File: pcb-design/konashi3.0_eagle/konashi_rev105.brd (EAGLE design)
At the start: 33 x 52.1 mm, 35 parts, among them CN1 ZX62-B-5PA(11), CN2 S2B-PH-K-S, CN3 WML-C69, CN4 MA05-2-2, CN7 BK-913, IC1 LP2981-30DBVR, IC2 ZLDO1117G50DITR-ND

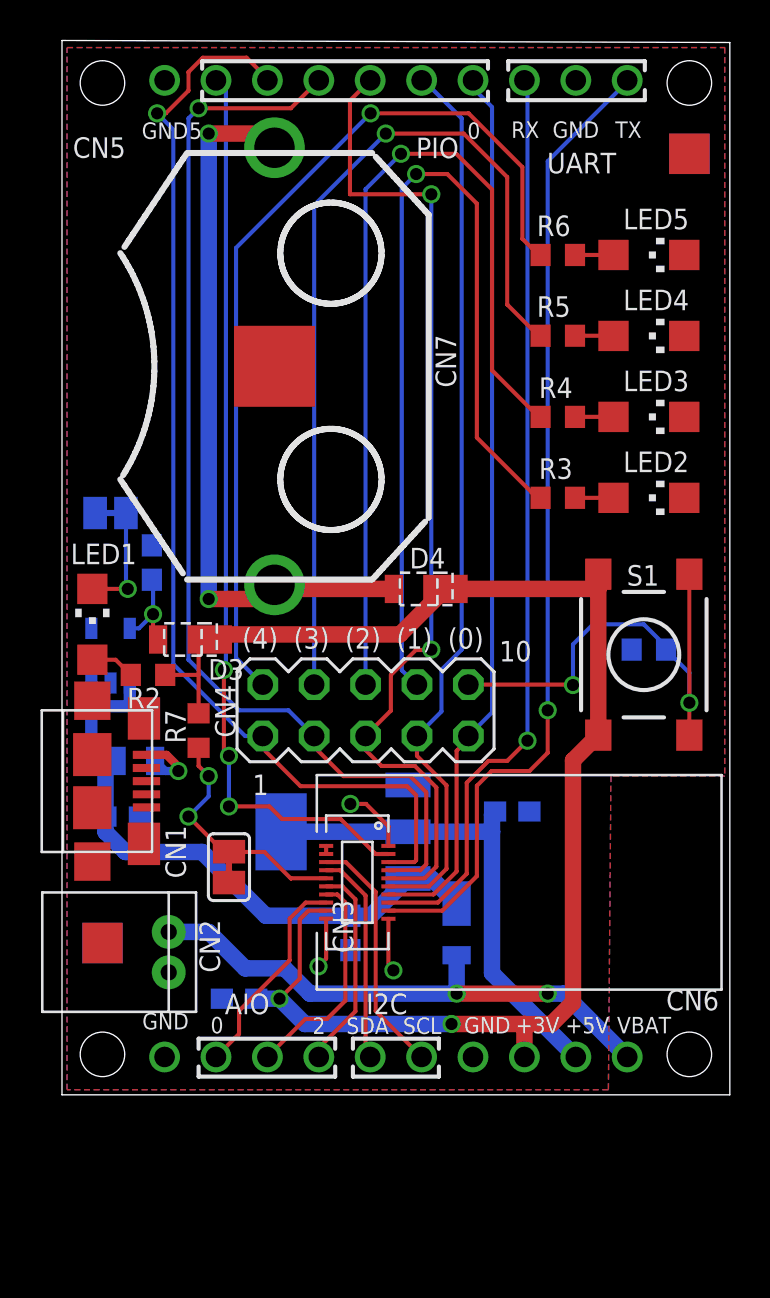
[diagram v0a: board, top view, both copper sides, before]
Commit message: 500kohm追加、ジャンパ用ピンヘッダ変更
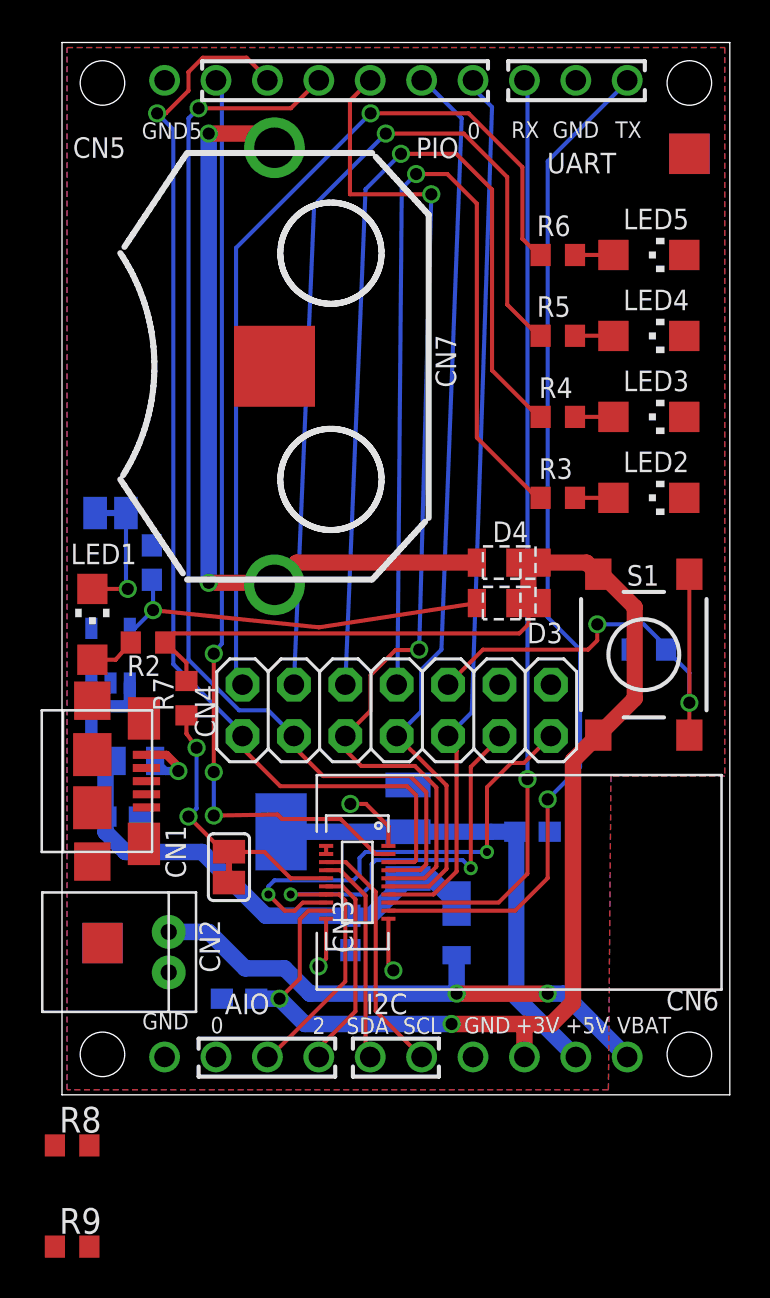
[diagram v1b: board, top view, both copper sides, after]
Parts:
- added R8, R9: 500k, rcl:R0603
- CN4: value MA05-2-2 -> 2X07; device con-std:MA05-2-2 -> konashi_rev105:2X07
- moved D3 15.9 mm to (22.1, 24.3)
- moved D4 4.30 mm to (22.1, 26.3)
- moved R7 1.71 mm to (6.15, 19.6)
- moved R2 1.60 mm to (4.25, 22.4)
- moved C5 1.41 mm to (23.2, 13.0)
- moved CN4 1.00 mm to (14.0, 19.0)
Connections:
- new net N$11: CN4.14, R9.1
- new net N$7: CN4.12, R8.1
- net AIO0: now also CN4.13
- net AIO1: now also CN4.11
- net GND: now also R8.2, R9.2
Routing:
- net AIO1: track 11.0 -> 29.7 mm, vias 0 -> 2
- net N$6: track 4.70 -> 19.2 mm
- net AIO0: track 10.5 -> 23.1 mm, vias 0 -> 2
- net N$4: track 36.3 -> 39.5 mm
- net TX: track 48.7 -> 51.0 mm
- net +3V: track 72.7 -> 74.7 mm
- net PIO2: track 50.1 -> 51.5 mm
- net N$5: track 12.1 -> 13.4 mm
- net RX: track 45.6 -> 46.8 mm
- net PIO5: track 45.1 -> 46.0 mm
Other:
- board size 33 x 52.1 mm -> 33 x 52 mm

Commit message: シルク修正
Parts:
- moved R9 40.3 mm to (24.1, 25.1), flipped to the bottom, turned to 90 degrees
- moved R8 34.8 mm to (21.6, 25.1), flipped to the bottom, turned to 90 degrees
- moved C5 2.40 mm to (23.2, 10.6)
- moved R2 0.80 mm to (4.25, 21.6)
- moved R7 0.60 mm to (6.15, 19.0)
- moved C1 0.40 mm to (4.44, 25.9)
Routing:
- net AIO0: track 23.1 -> 31.9 mm
- net N$7: track 0.00 -> 3.99 mm
- net N$11: track 0.00 -> 3.98 mm
- net PIO4: track 55.1 -> 52.3 mm
- net PIO2: track 51.5 -> 49.0 mm
- net N$23: track 45.3 -> 47.0 mm
- net PIO5: track 46.0 -> 47.7 mm, vias 3 -> 1
- net TX: track 51.0 -> 49.6 mm
- net +3V: track 74.7 -> 75.8 mm
- net GND: track 8.87 -> 7.76 mm
- net N$5: track 13.4 -> 12.5 mm
- net N$4: track 39.5 -> 38.7 mm
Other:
- board text added: "/SCL"
- board text added: "/SDA"
- board text added: "PIO6"
- board text added: "PIO7"
- board text added: "YE-WPC003"
- board text added: "rev. 1.05"
- board text removed: "I2C"
- board text removed: "SCL"
- board text removed: "SDA"
- board text removed: "YE-WPC002"
- board text removed: "rev. 1.03"

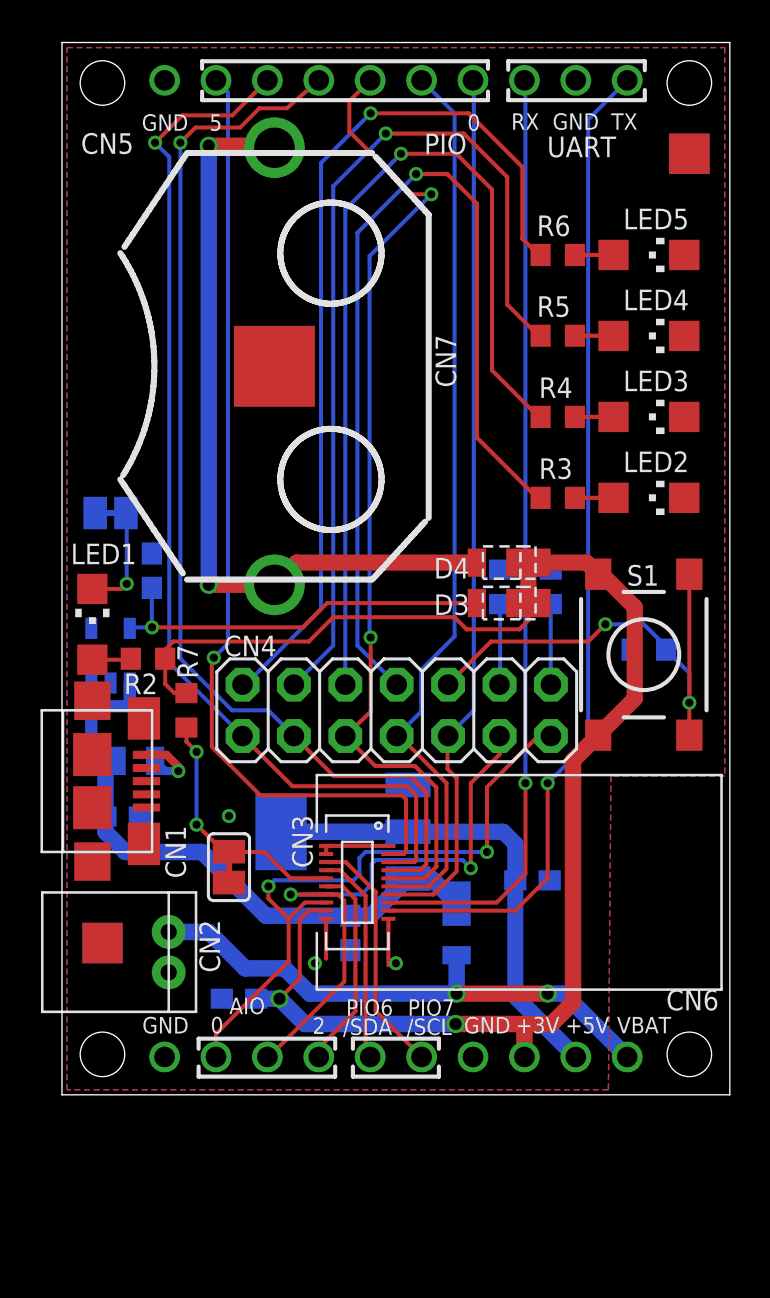
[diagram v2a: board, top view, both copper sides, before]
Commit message: ジャンパピンシルク追加等
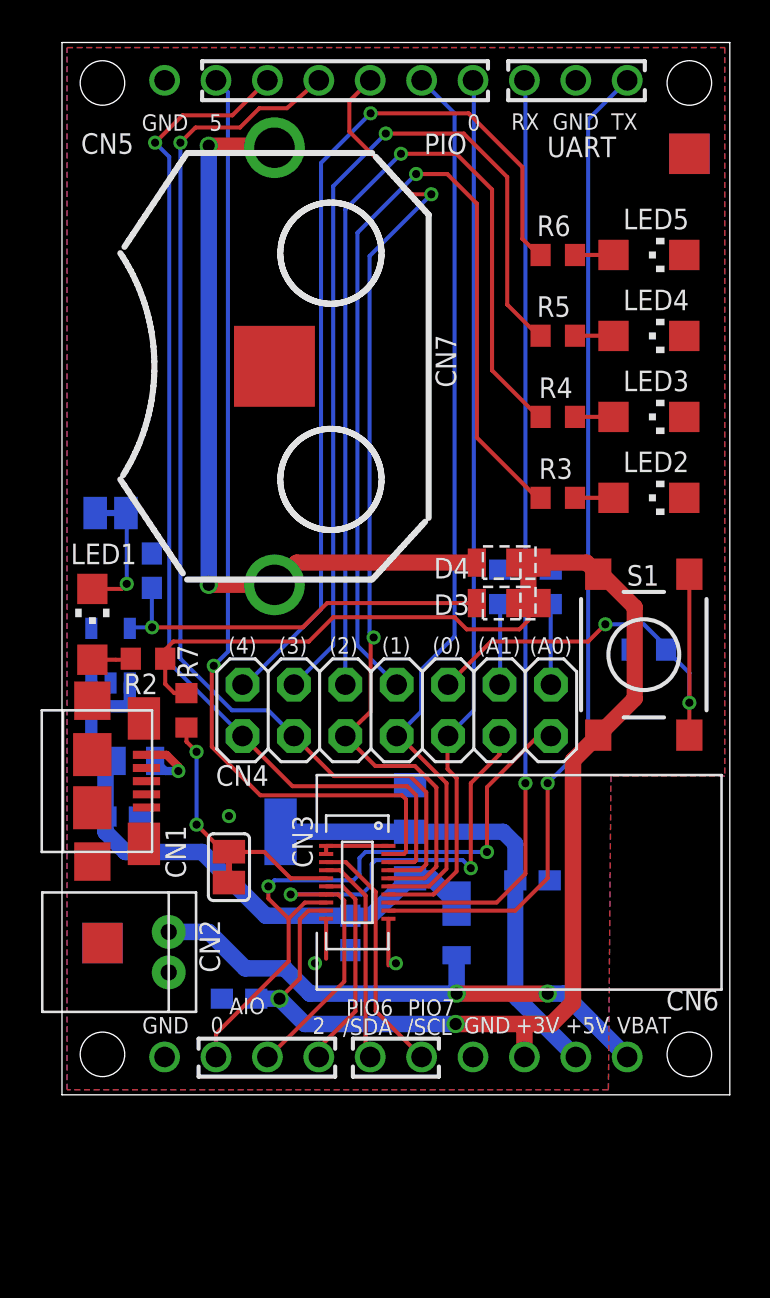
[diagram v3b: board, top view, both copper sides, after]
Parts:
- IC2: device LDO:SOT223 -> konashi_rev105:SOD233
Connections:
- net +5V: now also IC2.VOUT, IC2.VOUT2; no longer IC2.2, IC2.4
- net GND: now also IC2.GND; no longer IC2.1
- net N$8: now also IC2.VIN; no longer IC2.3
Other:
- board text added: "(0)"
- board text added: "(1)"
- board text added: "(2)"
- board text added: "(3)"
- board text added: "(4)"
- board text added: "(A0)"
- board text added: "(A1)"
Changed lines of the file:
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@@
 <layer number="20" name="Dimension" color="15" fill="1" visible="yes" active="yes"/>
 <layer number="21" name="tPlace" color="16" fill="1" visible="yes" active="yes"/>
-<layer number="22" name="bPlace" color="17" fill="1" visible="yes" active="yes"/>
-<layer number="23" name="tOrigins" color="16" fill="1" visible="yes" active="yes"/>
+<layer number="22" name="bPlace" color="17" fill="1" visible="no" active="yes"/>
+<layer number="23" name="tOrigins" color="16" fill="1" visible="no" active="yes"/>
 <layer number="24" name="bOrigins" color="17" fill="1" visible="yes" active="yes"/>
 <layer number="25" name="tNames" color="16" fill="1" visible="yes" active="yes"/>
@@
 <text x="14.9" y="4.82" size="0.8128" layer="22" font="vector" rot="MR180" align="bottom-center">PIO6</text>
 <text x="17.8" y="4.82" size="0.8128" layer="22" font="vector" rot="MR180" align="bottom-center">PIO7</text>
+<text x="18.3" y="21.8" size="0.8128" layer="25">(0)</text>
+<text x="15.8" y="21.8" size="0.8128" layer="25">(1)</text>
+<text x="13.2" y="21.8" size="0.8128" layer="25">(2)</text>
+<text x="10.7" y="21.8" size="0.8128" layer="25">(3)</text>
+<text x="8.2" y="21.8" size="0.8128" layer="25">(4)</text>
+<text x="23.1" y="21.8" size="0.8128" layer="25">(A0)</text>
+<text x="20.55" y="21.8" size="0.8128" layer="25">(A1)</text>
 </plain>
 <attributes>
@@
 </element>
 <element name="CN4" library="konashi_rev105" package="2X07" value="2X07" x="14" y="19" smashed="yes">
-<attribute name="NAME" x="7.999996875" y="21.6709875" size="1.016" layer="25" font="vector"/>
+<attribute name="NAME" x="7.599996875" y="15.2709875" size="1.016" layer="25" font="vector"/>
 </element>
 <element name="CN5" library="con-std" package="MA10-1" value="" x="16.5" y="50.13" smashed="yes" rot="R180">
@@
 <attribute name="NAME" x="22.415" y="9.564" size="0.8128" layer="26" font="vector" rot="MR180"/>
 </element>
-<element name="IC2" library="LDO" package="SOT223" value="ZLDO1117G50DITR-ND" x="14" y="13" smashed="yes" rot="MR270">
+<element name="IC2" library="konashi_rev105" package="SOD233" value="ZLDO1117G50DITR-ND" x="14" y="13" smashed="yes" rot="MR270">
 <attribute name="NAME" x="8.86" y="15.9492" size="0.8128" layer="26" font="vector" rot="MR180"/>
 </element>
@@
 <attribute name="NAME" x="18.46" y="37.56" size="1.016" layer="25" font="vector" rot="R270"/>
 </element>
-<element name="SJ2" library="pad" package="SJS" value="SJS" x="2.4" y="28.75" rot="MR180"/>
+<element name="SJ2" library="pad" package="SJS" value="SJS" x="2.4" y="28.75" smashed="yes" rot="MR180">
+<attribute name="NAME" x="0.349" y="27.607" size="1.016" layer="26" rot="MR180"/>
+<attribute name="VALUE" x="2.8001" y="28.75" size="0.02" layer="28" rot="MR180"/>
+</element>
 <element name="R8" library="rcl" package="R0603" value="500k" x="21.65" y="25.1" smashed="yes" rot="MR90">
 <attribute name="NAME" x="22.285" y="24.465" size="1.016" layer="26" font="vector" rot="MR90"/>
@@
 <contactref element="C4" pad="2"/>
 <contactref element="C5" pad="2"/>
-<contactref element="IC2" pad="1"/>
+<contactref element="IC2" pad="GND"/>
 <contactref element="CN6" pad="10"/>
 <contactref element="CN6" pad="4"/>
@@
 <signal name="N$8">
 <contactref element="C4" pad="1"/>
-<contactref element="IC2" pad="3"/>
+<contactref element="IC2" pad="VIN"/>
 <contactref element="D1" pad="C"/>
 <contactref element="D2" pad="C"/>
@@
 <wire x1="2.15" y1="16.5" x2="2.05" y2="16.5" width="0.8128" layer="16"/>
 <wire x1="14.25" y1="8.85" x2="15.2602" y2="8.85" width="0.8128" layer="16"/>
-<wire x1="15.2602" y1="8.85" x2="17.0988" y2="10.6886" width="0.8128" layer="16"/>
+<wire x1="15.2602" y1="8.85" x2="17.2" y2="10.7" width="0.8128" layer="16"/>
 <wire x1="19.5" y1="9.45" x2="18.2614" y2="10.6886" width="0.8128" layer="16"/>
-<wire x1="18.2614" y1="10.6886" x2="17.0988" y2="10.6886" width="0.8128" layer="16"/>
+<wire x1="18.2614" y1="10.6886" x2="17.2" y2="10.7" width="0.8128" layer="16"/>
 <contactref element="IC1" pad="1"/>
 <contactref element="IC1" pad="3"/>
@@
 <signal name="+5V">
 <contactref element="C5" pad="1"/>
-<contactref element="IC2" pad="2"/>
-<contactref element="IC2" pad="4"/>
+<contactref element="IC2" pad="VOUT"/>
+<contactref element="IC2" pad="VOUT2"/>
 <contactref element="CN6" pad="2"/>
-<wire x1="17.0988" y1="13" x2="10.825" y2="13" width="0.8128" layer="16"/>
+<wire x1="17.2" y1="13" x2="10.8" y2="13" width="0.8128" layer="16"/>
 <wire x1="25.39" y1="1.87" x2="22.53" y2="4.73" width="0.8128" layer="16"/>
 <wire x1="22.53" y1="4.73" x2="22.45" y2="4.81" width="0.8128" layer="16"/>
-<wire x1="17.0988" y1="13" x2="21.8" y2="13" width="0.8" layer="16"/>
+<wire x1="17.2" y1="13" x2="21.8" y2="13" width="0.8" layer="16"/>
 <wire x1="21.8" y1="13" x2="22.4" y2="12.4" width="0.8" layer="16"/>
 <wire x1="22.4" y1="12.4" x2="22.4" y2="10.599" width="0.8" layer="16"/>
@@
 <contactref element="CN3" pad="2"/>
 <contactref element="CN5" pad="9"/>
-<via x="7.5" y="21.6" extent="1-16" drill="0.4"/>
-<wire x1="8.2" y1="22.3" x2="8.2" y2="49.54" width="0.2" layer="16"/>
+<via x="7.5" y="21.2" extent="1-16" drill="0.4"/>
+<wire x1="8.2" y1="21.9" x2="8.2" y2="49.54" width="0.2" layer="16"/>
 <wire x1="8.2" y1="49.54" x2="7.61" y2="50.13" width="0.2" layer="16"/>
 <wire x1="16.1312" y1="11.9" x2="16.9" y2="11.9" width="0.2" layer="1"/>
@@
 <wire x1="16.8" y1="14.8" x2="9.8" y2="14.8" width="0.2" layer="1"/>
 <wire x1="9.8" y1="14.8" x2="7.4" y2="17.2" width="0.2" layer="1"/>
-<wire x1="7.4" y1="17.2" x2="7.4" y2="21.5" width="0.2" layer="1"/>
-<wire x1="7.4" y1="21.5" x2="7.5" y2="21.6" width="0.2" layer="1"/>
-<wire x1="8.2" y1="22.3" x2="7.5" y2="21.6" width="0.2" layer="16"/>
+<wire x1="7.4" y1="17.2" x2="7.4" y2="21.1" width="0.2" layer="1"/>
+<wire x1="7.4" y1="21.1" x2="7.5" y2="21.2" width="0.2" layer="1"/>
+<wire x1="8.2" y1="21.9" x2="7.5" y2="21.2" width="0.2" layer="16"/>
 </signal>
 <signal name="PIO3">
@@
 <wire x1="14.2" y1="47.6" x2="14.2" y2="49.1" width="0.2" layer="1"/>
 <wire x1="14.2" y1="49.1" x2="14.23" y2="49.13" width="0.2" layer="1"/>
-<wire x1="15.2" y1="22.65" x2="15.2" y2="41.45" width="0.2" layer="16"/>
-<wire x1="15.25" y1="18.93" x2="15.25" y2="22.6" width="0.2" layer="1"/>
-<via x="15.25" y="22.6" extent="1-16" drill="0.4"/>
-<wire x1="15.25" y1="22.6" x2="15.2" y2="22.65" width="0.2" layer="16"/>
+<wire x1="15.2" y1="22.85" x2="15.2" y2="41.45" width="0.2" layer="16"/>
+<wire x1="15.25" y1="18.93" x2="15.25" y2="22.45" width="0.2" layer="1"/>
+<wire x1="15.25" y1="22.45" x2="15.4" y2="22.6" width="0.2" layer="1"/>
+<via x="15.4" y="22.6" extent="1-16" drill="0.4"/>
+<wire x1="15.4" y1="22.6" x2="15.4" y2="22.65" width="0.2" layer="16"/>
+<wire x1="15.4" y1="22.65" x2="15.2" y2="22.85" width="0.2" layer="16"/>
 </signal>
 <signal name="PIO1">
